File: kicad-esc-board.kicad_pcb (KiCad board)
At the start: 2 copper layers, 105.2 x 32.1 mm, 9 parts, among them J1 PhoenixContact_01x03_WireToBo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, J2 PhoenixContact_01x02_WireToBo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, J3 Conn_01x01, J4 JST_01x02_TH_Vertical, J5 JST_01x02_TH_Vertical, M1 Blue Robotics Basic ESC

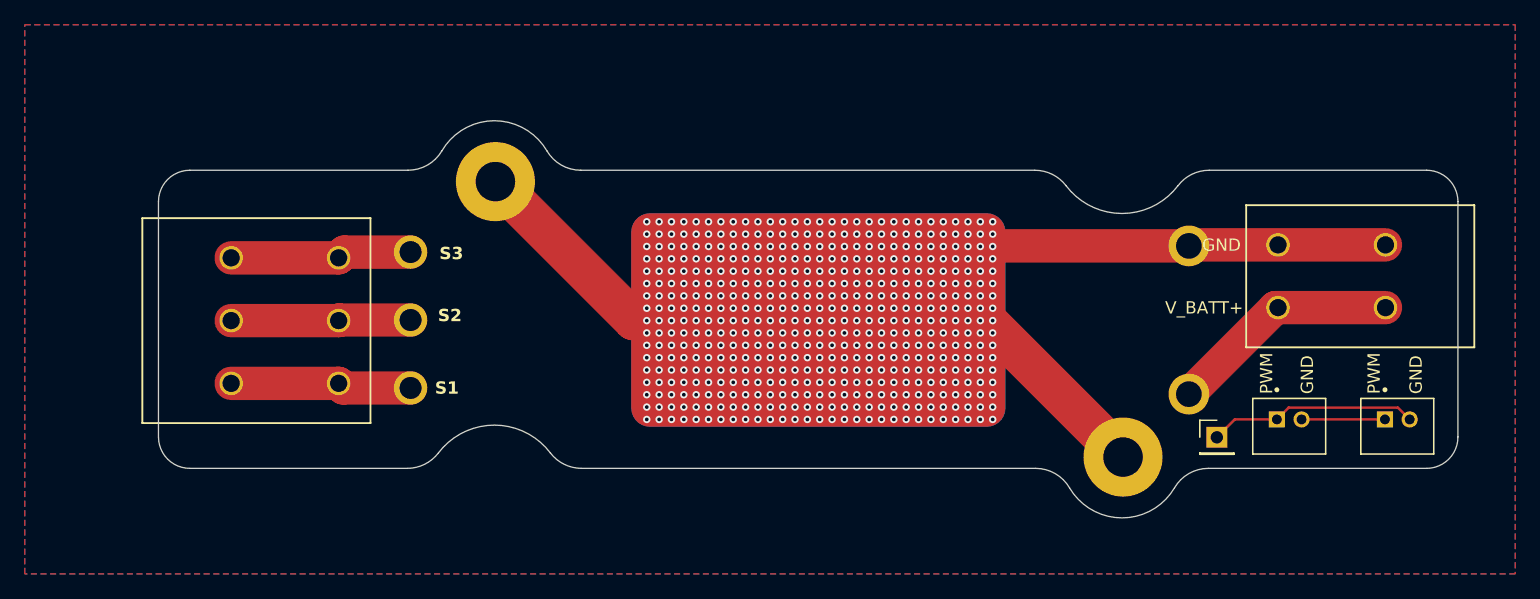
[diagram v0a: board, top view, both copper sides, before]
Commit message: Added the double pin header for logic analyzer testing and doubled up on power traces.
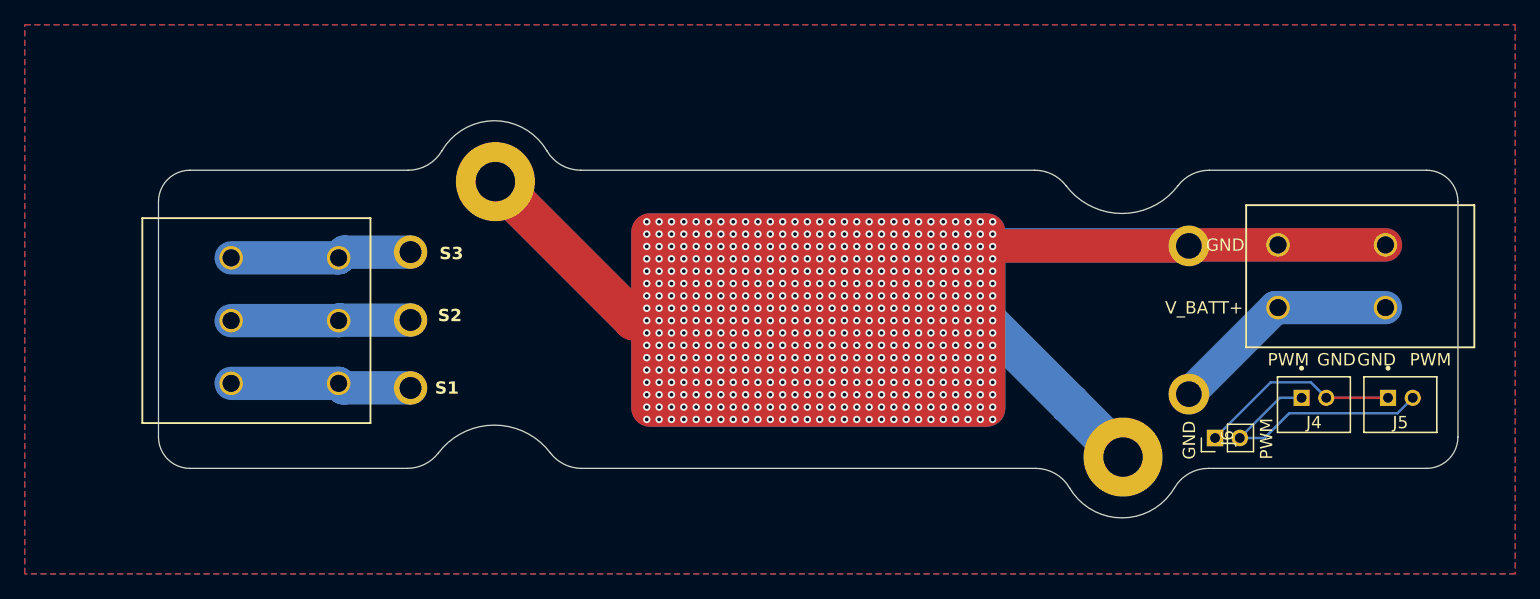
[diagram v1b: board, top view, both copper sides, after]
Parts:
- removed J3: Conn_01x01, Connector_PinHeader_2.54mm:PinHeader_1x01_P2.54mm_Vertical
- added J6: JST_01x02_TH_Vertical, Connector_PinHeader_2.00mm:PinHeader_1x02_P2.00mm_Vertical, F.Cu at (202.4, 96.0)
- moved J4 2.66 mm to (210.4, 93.3)
- moved J5 1.77 mm to (217.4, 93.3)
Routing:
- net GND: track 107.3 -> 219.0 mm
- net /PWM-GND: track 6.75 -> 21.6 mm
- net /PWM-Ctrl: track 17.0 -> 21.7 mm

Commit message: Made traces larger and added redundant traces
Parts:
- moved J4 1.52 mm to (210.7, 94.8)
- moved J5 1.50 mm to (217.4, 94.8)
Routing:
- net Net-(J2-Pin_1): track 18.8 -> 37.6 mm
- net Net-(J1-Pin_3): track 14.7 -> 29.4 mm
- net Net-(J1-Pin_1): track 14.7 -> 29.3 mm
- net Net-(J1-Pin_2): track 14.5 -> 29.1 mm
- net /PWM-Ctrl: track 21.7 -> 34.4 mm
- net /PWM-GND: track 21.6 -> 16.6 mm
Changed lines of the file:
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@@
 	(footprint "esc_board_custom_footprints:JST_B2B-PH-K-S"
 		(layer "F.Cu")
-		(at 210.4 93.34 180)
+		(at 210.65 94.84 180)
 		(property "Reference" "J4"
 			(at 0 -1.45 0)
@@
 	(footprint "esc_board_custom_footprints:JST_B2B-PH-K-S"
 		(layer "F.Cu")
-		(at 217.4 93.34 180)
+		(at 217.4 94.84 180)
 		(property "Reference" "J5"
 			(at 0 -1.45 0)
@@
 		)
 	)
-	(gr_text "PWM"
-		(at 206.65 90.29 0)
+	(gr_text "GND\n"
+		(at 200.9 97.79 90)
 		(layer "F.SilkS")
 		(effects
@@
 		)
 	)
-	(gr_text "GND\n"
-		(at 210.65 90.29 0)
+	(gr_text "PWM"
+		(at 207.15 97.79 90)
 		(layer "F.SilkS")
 		(effects
@@
 		)
 	)
-	(gr_text "GND\n"
-		(at 213.9 90.29 0)
+	(gr_text "PWM"
+		(at 210.15 92.29 90)
 		(layer "F.SilkS")
 		(effects
@@
 		)
 	)
-	(gr_text "PWM"
-		(at 218.15 90.29 0)
+	(gr_text "GND\n"
+		(at 212.4 92.29 90)
 		(layer "F.SilkS")
 		(effects
@@
 	)
 	(gr_text "GND\n"
-		(at 200.9 97.79 90)
+		(at 216.9 92.29 90)
 		(layer "F.SilkS")
 		(effects
@@
 	)
 	(gr_text "PWM"
-		(at 207.15 97.79 90)
+		(at 219.15 92.29 90)
 		(layer "F.SilkS")
 		(effects
@@
 	)
 	(segment
+		(start 207.494097 85.49)
+		(end 216.194099 85.49)
+		(width 3)
+		(layer "F.Cu")
+		(net "Net-(J2-Pin_1)")
+	)
+	(segment
+		(start 200.28 92.4925)
+		(end 200.491597 92.4925)
+		(width 2.7)
+		(layer "F.Cu")
+		(net "Net-(J2-Pin_1)")
+	)
+	(segment
+		(start 200.491597 92.4925)
+		(end 207.494097 85.49)
+		(width 3)
+		(layer "F.Cu")
+		(net "Net-(J2-Pin_1)")
+	)
+	(segment
 		(start 200.28 92.4925)
 		(end 207.2825 85.49)
@@
 	)
 	(segment
+		(start 137.28 91.9925)
+		(end 131.832502 91.9925)
+		(width 3)
+		(layer "F.Cu")
+		(net "Net-(J1-Pin_1)")
+	)
+	(segment
+		(start 131.832502 91.9925)
+		(end 131.460002 91.62)
+		(width 2.7)
+		(layer "F.Cu")
+		(net "Net-(J1-Pin_1)")
+	)
+	(segment
+		(start 131.460002 91.62)
+		(end 122.76 91.62)
+		(width 3)
+		(layer "F.Cu")
+		(net "Net-(J1-Pin_1)")
+	)
+	(segment
 		(start 131.832502 91.9925)
 		(end 131.460002 91.62)
@@
 		(start 122.76 86.54)
 		(end 131.460002 86.54)
+		(width 3)
+		(layer "F.Cu")
+		(net "Net-(J1-Pin_2)")
+	)
+	(segment
+		(start 137.2325 86.54)
+		(end 137.28 86.4925)
+		(width 2.7)
+		(layer "F.Cu")
+		(net "Net-(J1-Pin_2)")
+	)
+	(segment
+		(start 131.460002 86.54)
+		(end 137.2325 86.54)
+		(width 3)
+		(layer "F.Cu")
+		(net "Net-(J1-Pin_2)")
+	)
+	(segment
+		(start 122.76 86.54)
+		(end 131.460002 86.54)
 		(width 2.7)
 		(layer "B.Cu")
@@
 	)
 	(segment
+		(start 131.927502 80.9925)
+		(end 131.460002 81.46)
+		(width 2.7)
+		(layer "F.Cu")
+		(net "Net-(J1-Pin_3)")
+	)
+	(segment
+		(start 131.460002 81.46)
+		(end 122.76 81.46)
+		(width 3)
+		(layer "F.Cu")
+		(net "Net-(J1-Pin_3)")
+	)
+	(segment
+		(start 137.28 80.9925)
+		(end 131.927502 80.9925)
+		(width 3)
+		(layer "F.Cu")
+		(net "Net-(J1-Pin_3)")
+	)
+	(segment
 		(start 131.460002 81.46)
 		(end 122.76 81.46)
@@
 	)
 	(segment
-		(start 207.65 92.79)
-		(end 209.4 92.79)
+		(start 202.4 96.04)
+		(end 206.4 92.04)
 		(width 0.2)
 		(layer "B.Cu")
-		(net "/PWM-Ctrl")
+		(net "/PWM-GND")
 	)
 	(segment
-		(start 206.4 96.04)
-		(end 204.4 96.04)
+		(start 211.65 94.29)
+		(end 216.4 94.29)
 		(width 0.2)
 		(layer "B.Cu")
-		(net "/PWM-Ctrl")
+		(net "/PWM-GND")
 	)
 	(segment
-		(start 204.4 96.04)
-		(end 207.65 92.79)
+		(start 206.4 92.04)
+		(end 209.4 92.04)
 		(width 0.2)
 		(layer "B.Cu")
-		(net "/PWM-Ctrl")
+		(net "/PWM-GND")
 	)
 	(segment
-		(start 217.15 94.04)
-		(end 208.4 94.04)
+		(start 209.4 92.04)
+		(end 211.65 94.29)
 		(width 0.2)
 		(layer "B.Cu")
+		(net "/PWM-GND")
+	)
+	(segment
+		(start 207.9 96.04)
+		(end 209.65 94.29)
+		(width 0.2)
+		(layer "F.Cu")
 		(net "/PWM-Ctrl")
 	)
 	(segment
-		(start 218.4 92.79)
-		(end 217.15 94.04)
+		(start 218.4 94.29)
+		(end 216.65 96.04)
 		(width 0.2)
-		(layer "B.Cu")
+		(layer "F.Cu")
 		(net "/PWM-Ctrl")
 	)
 	(segment
-		(start 208.4 94.04)
-		(end 206.4 96.04)
+		(start 204.4 96.04)
+		(end 207.9 96.04)
 		(width 0.2)
-		(layer "B.Cu")
+		(layer "F.Cu")
 		(net "/PWM-Ctrl")
 	)
 	(segment
-		(start 211.15 92.79)
-		(end 216.4 92.79)
+		(start 216.65 96.04)
+		(end 207.9 96.04)
 		(width 0.2)
 		(layer "F.Cu")
-		(net "/PWM-GND")
+		(net "/PWM-Ctrl")
 	)
 	(segment
-		(start 210.15 91.54)
-		(end 206.9 91.54)
+		(start 218.4 94.29)
+		(end 216.65 96.04)
 		(width 0.2)
 		(layer "B.Cu")
-		(net "/PWM-GND")
+		(net "/PWM-Ctrl")
 	)
 	(segment
-		(start 211.4 92.79)
-		(end 210.15 91.54)
+		(start 216.65 96.04)
+		(end 207.9 96.04)
 		(width 0.2)
 		(layer "B.Cu")
-		(net "/PWM-GND")
+		(net "/PWM-Ctrl")
 	)
 	(segment
-		(start 206.9 91.54)
-		(end 202.4 96.04)
+		(start 207.9 96.04)
+		(end 204.4 96.04)
 		(width 0.2)
 		(layer "B.Cu")
-		(net "/PWM-GND")
+		(net "/PWM-Ctrl")
 	)
 	(segment
-		(start 216.4 92.79)
-		(end 211.4 92.79)
+		(start 209.65 94.29)
+		(end 207.9 96.04)
 		(width 0.2)
 		(layer "B.Cu")
-		(net "/PWM-GND")
+		(net "/PWM-Ctrl")
 	)
 	(zone

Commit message: made some final tweaks with net labels.
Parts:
- moved J5 0.25 mm to (217.7, 94.8)
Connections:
- J1 pad 4: Net-(J1-Pin_3) -> (no net)
- J5 pad 1: /PWM-GND -> /PWM-Ctrl
- J5 pad 2: /PWM-Ctrl -> /PWM-GND
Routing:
- net /PWM-Ctrl: track 34.4 -> 15.2 mm
- net /PWM-GND: track 16.6 -> 0.00 mm
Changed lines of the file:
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@@
 			(layers "*.Cu" "*.Mask")
 			(remove_unused_layers no)
-			(net "Net-(J1-Pin_3)")
 		)
 		(embedded_fonts no)
@@
 	(footprint "esc_board_custom_footprints:JST_B2B-PH-K-S"
 		(layer "F.Cu")
-		(at 217.4 94.84 180)
+		(at 217.65 94.84 180)
 		(property "Reference" "J5"
 			(at 0 -1.45 0)
@@
 			(layers "*.Cu" "*.Mask")
 			(remove_unused_layers no)
-			(net "/PWM-GND")
+			(net "/PWM-Ctrl")
 			(pinfunction "Pin_1_1")
 			(pintype "passive")
@@
 			(layers "*.Cu" "*.Mask")
 			(remove_unused_layers no)
-			(net "/PWM-Ctrl")
+			(net "/PWM-GND")
 			(pinfunction "Pin_2_2")
 			(pintype "passive")
@@
 		)
 	)
-	(gr_text "GND\n"
-		(at 216.9 92.29 90)
+	(gr_text "PWM"
+		(at 217.15 92.29 90)
 		(layer "F.SilkS")
 		(effects
@@
 		)
 	)
-	(gr_text "PWM"
+	(gr_text "GND\n"
 		(at 219.15 92.29 90)
 		(layer "F.SilkS")
@@
 	)
 	(segment
-		(start 202.4 96.04)
-		(end 206.4 92.04)
-		(width 0.2)
-		(layer "B.Cu")
-		(net "/PWM-GND")
-	)
-	(segment
-		(start 211.65 94.29)
-		(end 216.4 94.29)
-		(width 0.2)
-		(layer "B.Cu")
-		(net "/PWM-GND")
-	)
-	(segment
-		(start 206.4 92.04)
-		(end 209.4 92.04)
-		(width 0.2)
-		(layer "B.Cu")
-		(net "/PWM-GND")
-	)
-	(segment
-		(start 209.4 92.04)
-		(end 211.65 94.29)
-		(width 0.2)
-		(layer "B.Cu")
-		(net "/PWM-GND")
-	)
-	(segment
-		(start 207.9 96.04)
-		(end 209.65 94.29)
-		(width 0.2)
-		(layer "F.Cu")
-		(net "/PWM-Ctrl")
-	)
-	(segment
-		(start 218.4 94.29)
-		(end 216.65 96.04)
-		(width 0.2)
+		(start 209.65 94.29)
+		(end 209.65 93.79)
+		(width 0.4)
 		(layer "F.Cu")
 		(net "/PWM-Ctrl")
@@
 	(segment
 		(start 204.4 96.04)
-		(end 207.9 96.04)
-		(width 0.2)
+		(end 206.15 94.29)
+		(width 0.4)
 		(layer "F.Cu")
 		(net "/PWM-Ctrl")
 	)
 	(segment
-		(start 216.65 96.04)
-		(end 207.9 96.04)
-		(width 0.2)
+		(start 206.15 94.29)
+		(end 209.65 94.29)
+		(width 0.4)
 		(layer "F.Cu")
 		(net "/PWM-Ctrl")
 	)
 	(segment
-		(start 218.4 94.29)
-		(end 216.65 96.04)
-		(width 0.2)
-		(layer "B.Cu")
+		(start 215.15 92.29)
+		(end 216.65 93.79)
+		(width 0.4)
+		(layer "F.Cu")
 		(net "/PWM-Ctrl")
 	)
 	(segment
-		(start 216.65 96.04)
-		(end 207.9 96.04)
-		(width 0.2)
-		(layer "B.Cu")
+		(start 209.65 93.79)
+		(end 211.15 92.29)
+		(width 0.4)
+		(layer "F.Cu")
 		(net "/PWM-Ctrl")
 	)
 	(segment
-		(start 207.9 96.04)
-		(end 204.4 96.04)
-		(width 0.2)
-		(layer "B.Cu")
+		(start 216.65 93.79)
+		(end 216.65 94.29)
+		(width 0.4)
+		(layer "F.Cu")
 		(net "/PWM-Ctrl")
 	)
 	(segment
-		(start 209.65 94.29)
-		(end 207.9 96.04)
-		(width 0.2)
-		(layer "B.Cu")
+		(start 211.15 92.29)
+		(end 215.15 92.29)
+		(width 0.4)
+		(layer "F.Cu")
 		(net "/PWM-Ctrl")
 	)

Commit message: made common grounds between PWM connections and board.
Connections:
- J1 pad 4: (no net) -> Net-(J1-Pin_3)
- J4 pad 2: /PWM-GND -> GND
- J5 pad 2: /PWM-GND -> GND
- J6 pad 1: /PWM-GND -> GND
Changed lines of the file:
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@@
 			(layers "*.Cu" "*.Mask")
 			(remove_unused_layers no)
+			(net "Net-(J1-Pin_3)")
 		)
 		(embedded_fonts no)
@@
 			(layers "*.Cu" "*.Mask")
 			(remove_unused_layers no)
-			(net "/PWM-GND")
+			(net "GND")
 			(pinfunction "Pin_1_1")
 			(pintype "passive")
@@
 			(layers "*.Cu" "*.Mask")
 			(remove_unused_layers no)
-			(net "/PWM-GND")
+			(net "GND")
 			(pinfunction "Pin_2_2")
 			(pintype "passive")
@@
 			(layers "*.Cu" "*.Mask")
 			(remove_unused_layers no)
-			(net "/PWM-GND")
+			(net "GND")
 			(pinfunction "Pin_2_2")
 			(pintype "passive")
